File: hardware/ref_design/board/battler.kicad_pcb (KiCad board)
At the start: 4 copper layers, 70.4 x 151.2 mm, 123 parts, among them J1 TYPE-C-31-M-12, J2 S2B-PH-SM4-TB, J3 QD3525, J4 SPEAKER, J5 SWD, J6 UART, Q1 2N7002, SW1 P1 UP, SW10 P2 DOWN, SW11 P2 LEFT, SW12 P2 RIGHT, SW13 P2 A, SW14 P2 B, SW15 P2 X, SW16 P2 Y, SW17 PWR, SW18 BOOTSEL, SW19 RESET, SW2 P1 DOWN, SW3 P1 LEFT, SW4 P1 RIGHT, SW5 P1 A, SW6 P1 B, SW7 P1 X, SW8 P1 Y, SW9 P2 UP, U1 USBLC6-2SC6, U2 BQ24074RGTR, U3 TPS63001DRCR, U4 RP2350B, U5 W25Q128JVPIQ, U6 AP3156FVG-7, U7 MAX98357AETE+T, X1 12MHz

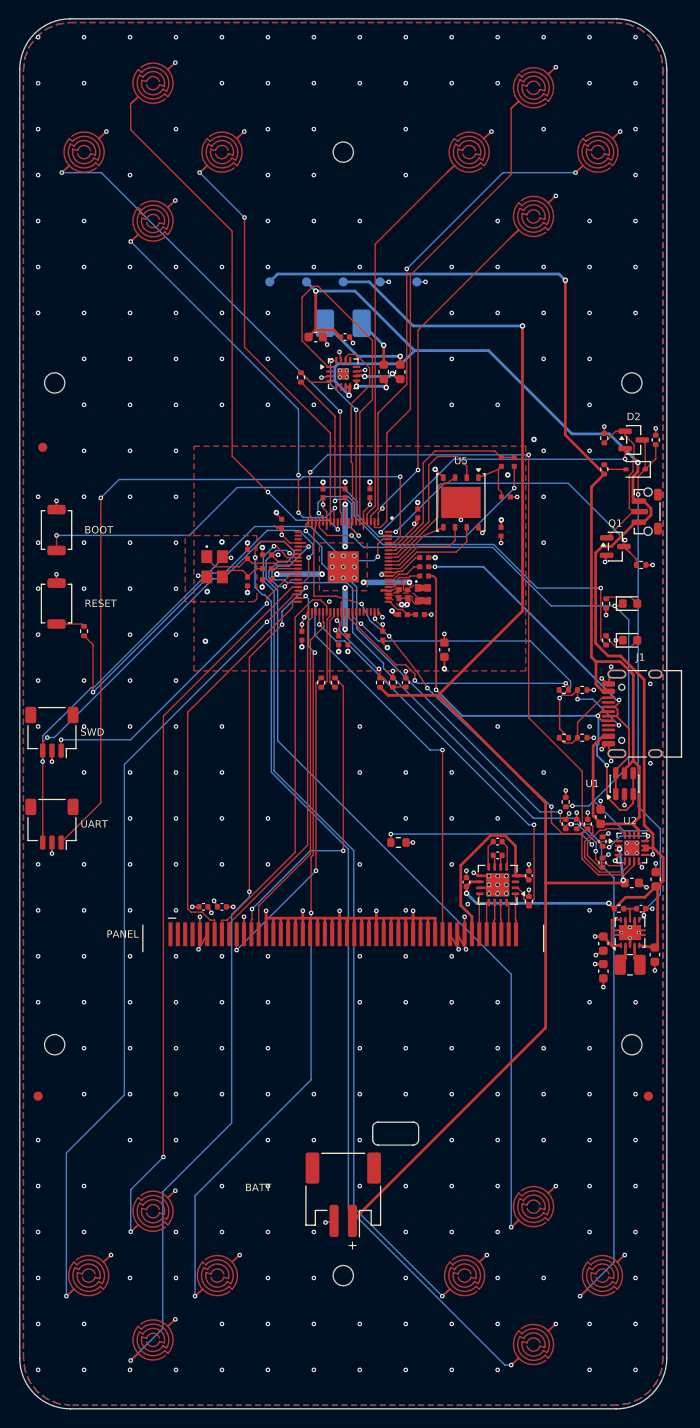
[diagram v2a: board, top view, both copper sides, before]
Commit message: 2-layer fork: board, case and docs for the approved cost changes
Board on two layers with every hole >= 0.3 mm (JLC's standard; smaller holes
cost about $40 an order), routed DRC-clean: 0 errors, 0 unconnected, 0 parity.
The RP2354B core is Raspberry Pi's 2-layer layout; its 3V3 pour sits inside
the chip's pads, fenced from the router, and every 3V3 pin stubs into it. GND
is poured on both layers and left out of Freerouting's job; 3V3 is routed.
USB series resistors are 22 ohm 0402 in Raspberry Pi's spots (a 27 ohm 0603
doesn't fit); UART1 on GPIO20/21 and seat 1's right on GPIO23 escape the
crystal's corner. route.py --finish closes what a full run leaves open.

Case 15 mm thick for the 503450 cell; the lid snaps on six hooks, six pins
locate the board; no lens, light pipes or power cap. Fit check: 90 parts, no
collisions. BOM split into factory (about $15.10 a unit) and self-assembled
(about $14-18); assembly, bring-up, pin map and design review updated.

Co-Authored-By: Claude Opus 5.5 <noreply@anthropic.com>
Claude-Session: https://claude.ai/code/session_01KGgEu3CbFtCsvHRQgAFiCN
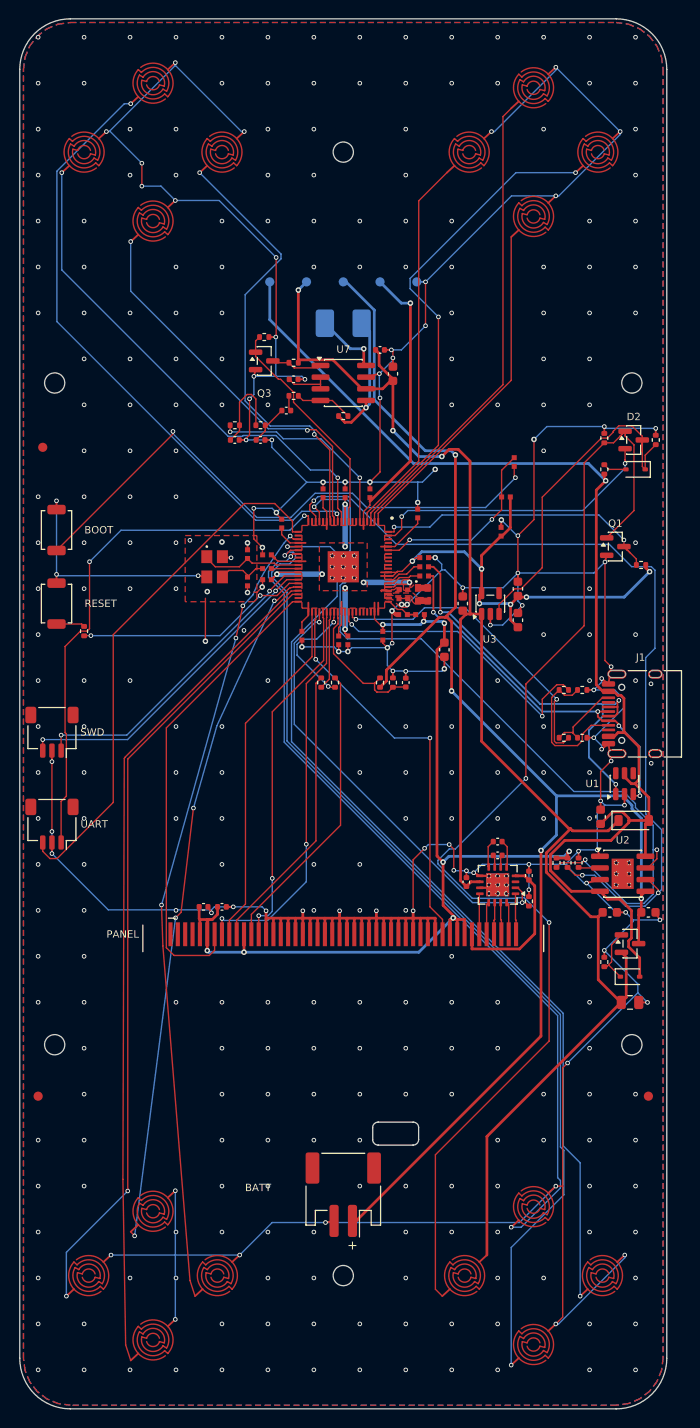
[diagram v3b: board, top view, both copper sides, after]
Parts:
- removed C4: 100n, Capacitor_SMD:C_0402_1005Metric
- removed D1: amber, LED_SMD:LED_0603_1608Metric
- removed D4: red, LED_SMD:LED_0603_1608Metric
- removed FB1, FB2: 120R@100MHz, Inductor_SMD:L_0603_1608Metric
- removed L1: 2.2u, Inductor_SMD:L_1008_2520Metric
- removed R11, R27: 1k, Resistor_SMD:R_0402_1005Metric
- removed R12: 100, Resistor_SMD:R_0402_1005Metric
- removed R24: 0, battler:R_0402_1005Metric_RPi
- removed R7, R8: 100k, Resistor_SMD:R_0402_1005Metric
- removed RT1: 10k B3380, Resistor_SMD:R_0603_1608Metric
- removed SW17: PWR, battler:SW_Alps_SKRTLAE010_Pullback
- removed U5: W25Q128JVPIQ, Package_SON:WSON-8-1EP_6x5mm_P1.27mm_EP3.4x4.3mm
- added C37: 10n, Capacitor_SMD:C_0402_1005Metric, F.Cu at (88.2, 70.2)
- added C38: 10n, Capacitor_SMD:C_0402_1005Metric, F.Cu at (91.0, 70.2)
- added C39: 220n, Capacitor_SMD:C_0402_1005Metric, F.Cu at (93.8, 67.0)
- added C40: 1u, Capacitor_SMD:C_0402_1005Metric, F.Cu at (94.6, 63.6)
- added C9: 22u, Capacitor_SMD:C_0805_2012Metric, F.Cu at (131.2, 131.4)
- added D5: B5819W, Diode_SMD:D_SOD-123, F.Cu at (131.6, 111.6)
- added D6: BAT54WS, Diode_SMD:D_SOD-323, F.Cu at (131.2, 128.6)
- added Q2: AO3401A, Package_TO_SOT_SMD:SOT-23, F.Cu at (131.2, 125.0)
- added Q3: 2N7002, Package_TO_SOT_SMD:SOT-23, F.Cu at (91.4, 61.6)
- added R33: 1k, Resistor_SMD:R_0402_1005Metric, F.Cu at (91.0, 68.6)
- added R34: 20k, Resistor_SMD:R_0402_1005Metric, F.Cu at (94.6, 65.4)
- added R35: 20k, Resistor_SMD:R_0402_1005Metric, F.Cu at (100.0, 67.6)
- added R36: 100k, Resistor_SMD:R_0402_1005Metric, F.Cu at (94.6, 61.8)
- added R37: 100k, Resistor_SMD:R_0402_1005Metric, F.Cu at (91.4, 59.0)
- C3: value 4.7u -> 10u
- R21, R22: value 27 -> 22
- R32: value 47k -> 1k
- R5: value 1.2k -> 2.4k
- R6: value 1.2k -> 10k
- SW8: value P1 Y -> P1 Y / PWR
- U1: value USBLC6-2SC6 -> SRV05-4
- U2: value BQ24074RGTR -> TP4056-42-ESOP8; footprint Package_DFN_QFN:VQFN-16-1EP_3x3mm_P0.5mm_EP1.6x1.6mm_ThermalVias -> battler:SOIC-8-1EP_3.9x4.9mm_P1.27mm_EP2.41x3.3mm_ThermalVias_0.3mm
- U3: value TPS63001DRCR -> ME6211C33M5G; footprint Package_SON:Texas_DRC0010J_ThermalVias -> Package_TO_SOT_SMD:SOT-23-5
- U4: value RP2350B -> RP2354B
- U7: value MAX98357AETE+T -> FM8002A; footprint Package_DFN_QFN:TQFN-16-1EP_3x3mm_P0.5mm_EP1.23x1.23mm_ThermalVias -> Package_SO:SOIC-8_3.9x4.9mm_P1.27mm
- moved C5 43.5 mm to (113.0, 88.0), turned to 90 degrees
- moved C6 39.7 mm to (119.0, 86.4), turned to 90 degrees
- moved C7 39.3 mm to (119.0, 89.8), turned to 90 degrees
- moved U3 38.9 mm to (116.0, 88.0)
- moved R6 10.8 mm to (128.4, 127.0)
- moved C34 9.30 mm to (105.4, 63.0), turned to 90 degrees
- moved R32 8.88 mm to (88.2, 68.6), turned to 0 degrees
- moved R10 6.68 mm to (123.2, 116.2)
- moved C2 6.16 mm to (129.0, 121.6), turned to 0 degrees
- moved R9 4.74 mm to (124.4, 116.2)
- moved C35 4.05 mm to (104.0, 60.4)
- moved C3 3.67 mm to (133.2, 121.6)
- moved R5 3.47 mm to (125.6, 116.2)
- moved U2 2.97 mm to (130.4, 117.4)
- moved U7 1.00 mm to (100.0, 64.0)
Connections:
- D2 pad 1: /Power/PWR_BTN_RAW -> PWR_BTN_RAW
- Q1 pad 1: /Power/PWR_BTN_RAW -> PWR_BTN_RAW
- R13 pad 1: /Power/PWR_BTN_RAW -> PWR_BTN_RAW
- R23 pad 2: /MCU/FLASH_SS -> QSPI_SS
- R32 pad 1: AMP_SD -> AUDIO_PWM
- R32 pad 2: /Audio/AMP_SD_MODE -> /Audio/AUDIO_F1
- R5 pad 1: /USB_Charger/ILIM -> /USB_Charger/CHG_PROG
- R6 pad 1: /USB_Charger/ISET -> /USB_Charger/LS_GATE
- R9 pad 1: VIN_GOOD_N -> CHG_DONE_N
- SW8 pad 1: P1_Y -> PWR_BTN_RAW
- SW8 pad 2: GND -> VSYS
- U1 pad 4: USB_DM -> (no net)
- U1 pad 6: USB_DP -> (no net)
- U2 pad 1: /USB_Charger/TS -> GND
- U2 pad 2: VBAT -> /USB_Charger/CHG_PROG
- U2 pad 3: VBAT -> GND
- U2 pad 4: GND -> VBUS
- U2 pad 5: CHG_EN2 -> VBAT
- U2 pad 6: CHG_EN1 -> CHG_DONE_N
- U2 pad 7: VIN_GOOD_N -> CHG_STAT_N
- U2 pad 8: GND -> VBUS
- U2 pad 9: CHG_STAT_N -> GND
- U3 pad 1: +3V3 -> VSYS
- U3 pad 2: /Power/BB_L2 -> GND
- U3 pad 3: GND -> /Power/PWR_EN
- U3 pad 4: /Power/BB_L1 -> (no net)
- U3 pad 5: VSYS -> +3V3
- U4 pad 16: STATUS_LED -> (no net)
- U4 pad 18: VIN_GOOD_N -> CHG_DONE_N
- U4 pad 19: CHG_EN1 -> (no net)
- U4 pad 20: CHG_EN2 -> UART_TX
- U4 pad 21: (no net) -> UART_RX
- U4 pad 23: (no net) -> P1_RIGHT
- U4 pad 28: P1_Y -> (no net)
- U4 pad 39: P1_RIGHT -> (no net)
- U4 pad 6: I2S_DIN -> AUDIO_PWM
- U4 pad 7: I2S_BCLK -> (no net)
- U4 pad 70: /MCU/QSPI_SD3 -> (no net)
- U4 pad 71: /MCU/QSPI_SCLK -> (no net)
- U4 pad 72: /MCU/QSPI_SD0 -> (no net)
- U4 pad 73: /MCU/QSPI_SD2 -> (no net)
- U4 pad 74: /MCU/QSPI_SD1 -> (no net)
- U4 pad 77: UART_TX -> (no net)
- U4 pad 78: UART_RX -> (no net)
- U4 pad 8: I2S_LRCLK -> (no net)
- U4 pad 9: AMP_SD -> AMP_EN
- U7 pad 1: I2S_DIN -> /Audio/AMP_SHDN
- U7 pad 2: (no net) -> /Audio/AMP_BYP
- U7 pad 3: GND -> /Audio/AMP_BYP
- U7 pad 4: /Audio/AMP_SD_MODE -> /Audio/AMP_INN
- U7 pad 5: (no net) -> /Audio/SPK_P
- U7 pad 6: (no net) -> VSYS
- U7 pad 7: VSYS -> GND
- U7 pad 8: VSYS -> /Audio/SPK_N
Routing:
- net GND: track 153.9 -> 692.9 mm, vias 355 -> 361
- net +3V3: track 75.6 -> 218.9 mm, vias 35 -> 15
- net PWR_BTN_RAW: track 0.00 -> 133.7 mm, vias 0 -> 2
- net P1_Y: track 94.5 -> 0.00 mm, vias 2 -> 0
- net CHG_DONE_N: track 0.00 -> 94.2 mm, vias 0 -> 3
- net CHG_EN1: track 86.1 -> 0.00 mm, vias 2 -> 0
- net VIN_GOOD_N: track 61.0 -> 0.00 mm, vias 4 -> 0
- net CHG_EN2: track 57.3 -> 0.00 mm, vias 4 -> 0
- net STATUS_LED: track 44.8 -> 0.00 mm, vias 2 -> 0
- net I2S_DIN: track 39.9 -> 0.00 mm
- net VSYS: track 157.3 -> 190.0 mm, vias 5 -> 3
- net /USB_Charger/TS: track 26.3 -> 0.00 mm, vias 2 -> 0
- net AMP_EN: track 0.00 -> 24.7 mm
- net AMP_SD: track 22.4 -> 0.00 mm, vias 2 -> 0
- net UART_TX: track 80.9 -> 58.9 mm
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- removed copper zone on In2.Cu, net +3V3
- removed copper zone on In1.Cu, net GND
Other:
- copper layers 4 -> 2
- board text added: "2 LAYERS 1.6 MM ENIG"
- board text removed: "4 LAYERS 1.6 MM ENIG"

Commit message: Reference design: plug-in ER-TFT035IPS-6 panel, pins and pin escapes for 2 layers
- Panel: EastRising ER-TFT035IPS-6 (ILI9488, 320x480 IPS) on a Hirose FH12-50S
  ZIF connector (J3) that JLC places, instead of the QD3525's hand-soldered tail.
  Case panel/FPC geometry, fit check (FPC zones), backlight sinks paired onto
  its two cathode pins, docs and BOM updated. Prices from both shops' carts:
  about $14.20 a unit at 10 with shipping.
- Pins reassigned for two layers: each faces where its net goes, in fan-out
  order (seat 1's face buttons, panel reset, backlight and ADC inputs on
  GPIO40-47; seat 1's cross and the panel's TE on GPIO28-32).
- build_pcb.copy_escapes: Raspberry Pi's own routing out of the RP2354B's pins,
  copied with the core and locked, so no pin gets boxed in by its neighbours.
  The board now routes completely in about 10 minutes.
- route.py: loose tracks are trimmed back to their last real join instead of
  deleted (Freerouting meets stubs part-way along), T-joins are split and
  duplicate tracks dropped; Freerouting routes to +5 um clearance and a 0.12 mm
  inset outline (it rounded under 0.15 mm and hugged the board edge).
- MCU sheet region widened for the longer labels; datasheet list updated for
  the 2-layer parts; old panel landing footprint/tool and the unused side
  switch footprint removed.

Checks: netlist PASS (122 parts, 115 nets), ERC 0, DRC 0 errors / 0
unconnected / 0 parity (2 cosmetic silk warnings), holes 0.3/0.6/0.65/2.2 mm,
fit PASS on 91 parts.

Co-Authored-By: Claude Opus 5.5 <noreply@anthropic.com>
Claude-Session: https://claude.ai/code/session_01KGgEu3CbFtCsvHRQgAFiCN
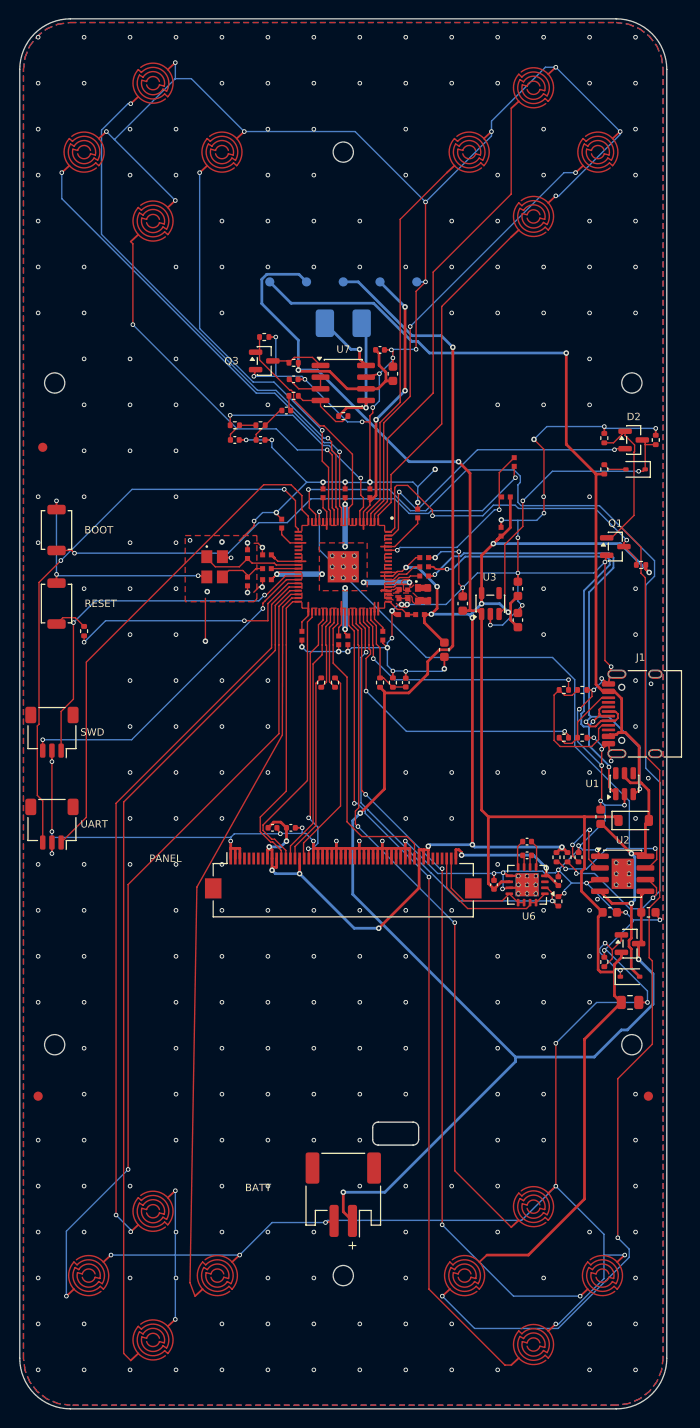
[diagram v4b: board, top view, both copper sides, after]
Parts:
- J3: value QD3525 -> FH12-50S-0.5SH(55); footprint battler:QD3525_FPC_1x48_P0.80mm_Solder -> Connector_FFC-FPC:Hirose_FH12-50S-0.5SH_1x50-1MP_P0.50mm_Horizontal
- moved C29 11.4 mm to (92.3, 112.4)
- moved C30 11.4 mm to (94.3, 112.4)
- moved J3 6.39 mm to (100.0, 117.6)
- moved C32 3.26 mm to (123.4, 118.2)
- moved C33 3.20 mm to (120.0, 115.4)
- moved C36 3.20 mm to (120.0, 113.9)
- moved R31 3.20 mm to (123.4, 120.4)
- moved U6 3.20 mm to (120.0, 118.6)
- moved C31 3.01 mm to (116.4, 118.6)
- moved R10 0.60 mm to (123.2, 115.6)
- moved R5 0.60 mm to (125.6, 115.6)
- moved R9 0.60 mm to (124.4, 115.6)
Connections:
- J3 pad 1: (no net) -> GND
- J3 pad 10: /Display/LCD_SCK -> +3V3
- J3 pad 12: /Display/LCD_MOSI -> LCD_TE
- J3 pad 13: LCD_MISO -> LCD_CS
- J3 pad 14: GND -> LCD_DC
- J3 pad 15: GND -> /Display/LCD_SCK
- J3 pad 16: GND -> +3V3
- J3 pad 17: GND -> /Display/LCD_MOSI
- J3 pad 18: GND -> LCD_MISO
- J3 pad 2: (no net) -> GND
- J3 pad 3: (no net) -> GND
- J3 pad 38: LCD_RST -> GND
- J3 pad 39: +3V3 -> GND
- J3 pad 40: +3V3 -> GND
- J3 pad 41: +3V3 -> LCD_RST
- J3 pad 42: /Display/LED_A -> +3V3
- J3 pad 43: /Display/LED_K1 -> +3V3
- J3 pad 44: /Display/LED_K2 -> +3V3
- J3 pad 45: /Display/LED_K3 -> (no net)
- J3 pad 46: /Display/LED_K4 -> (no net)
- J3 pad 47: /Display/LED_K5 -> (no net)
- J3 pad 48: /Display/LED_K6 -> /Display/LED_K2
- J3 pad 5: +3V3 -> (no net)
- J3 pad 6: +3V3 -> (no net)
- J3 pad 7: LCD_TE -> (no net)
- J3 pad 8: LCD_CS -> GND
- J3 pad 9: LCD_DC -> +3V3
- U4 pad 23: P1_RIGHT -> (no net)
- U4 pad 25: P1_A -> (no net)
- U4 pad 26: P1_B -> (no net)
- U4 pad 27: P1_X -> (no net)
- U4 pad 39: (no net) -> P1_RIGHT
- U4 pad 42: LCD_DC -> LCD_CS
- U4 pad 43: LCD_RST -> (no net)
- U4 pad 44: BL_SDI -> (no net)
- U4 pad 46: LCD_CS -> LCD_DC
- U4 pad 49: VBAT_SENSE -> LCD_RST
- U4 pad 52: CC1_SENSE -> P1_B
- U4 pad 53: CC2_SENSE -> P1_X
- U4 pad 54: (no net) -> P1_A
- U4 pad 55: (no net) -> BL_SDI
- U4 pad 56: (no net) -> CC2_SENSE
- U4 pad 57: (no net) -> CC1_SENSE
- U4 pad 58: (no net) -> VBAT_SENSE
- U6 pad 1: /Display/LED_K6 -> /Display/LED_K2
- U6 pad 13: /Display/LED_K2 -> /Display/LED_K1
- U6 pad 14: /Display/LED_K3 -> /Display/LED_K1
- U6 pad 15: /Display/LED_K4 -> /Display/LED_K2
- U6 pad 16: /Display/LED_K5 -> /Display/LED_K2
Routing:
- net LCD_TE: track 51.5 -> 31.1 mm
- net P1_B: track 109.7 -> 91.0 mm
- net USB_DM: track 40.8 -> 58.4 mm, vias 4 -> 3
- net P1_X: track 92.6 -> 75.6 mm
- net P1_A: track 103.9 -> 90.1 mm, vias 2 -> 4
- net GND: track 692.9 -> 679.8 mm, vias 361 -> 357
- net LCD_CS: track 43.0 -> 30.3 mm, vias 2 -> 0
- net CHG_STAT_N: track 87.9 -> 75.6 mm
- net /Display/LED_K2: track 3.62 -> 15.6 mm
- net /Display/LCD_SCK: track 31.7 -> 20.8 mm
- net /Display/LCD_MOSI: track 32.2 -> 21.6 mm
- net LCD_DC: track 38.8 -> 28.5 mm
- net LCD_MISO: track 38.6 -> 28.6 mm
- net VBUS: track 134.2 -> 124.6 mm, vias 1 -> 3
- net LCD_RST: track 43.1 -> 33.6 mm, vias 2 -> 0
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
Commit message: Reference design: audit round 1 fixes (USB ESD reference, PWR_EN pull-down)
From an independent audit of the 2-layer board:
- SRV05-4 REF (U1 pin 5) moves from VBUS to 3V3. On VBUS, with no cable in,
  the MCU's D+ pull-up (always on in BOOTSEL mode) fed VBUS through the D+
  steering diode to about 2.7 V: PWR_EN stayed up, so the device could not
  turn off, and the load-sharing FET was left half on.
- R15 (PWR_EN pull-down) 100k -> 10k, so D5's reverse leakage into the VBUS
  node can't lift the ME6211's CE to 1.0 V when warm.
- J6 (UART) turned 180 degrees: its mouth faced J5's back 5 mm away.
- Lid: the panel's locating frame gets 0.8 mm clearance (panel_fit), not 0.4.
- Docs: ILI9488 reads at 5 MHz or less, TP4056 current 460-500 mA and its
  145 C thermal limit, how 3V3 reaches the core pour, FPC insertion depth and
  expected slack, JLC's 374 solder joints, board size as quoted.

Checks: netlist PASS, ERC 0, DRC 0 errors / 0 unconnected / 0 parity
(2 cosmetic silk warnings), fit PASS on 91 parts.

Co-Authored-By: Claude Opus 5.5 <noreply@anthropic.com>
Claude-Session: https://claude.ai/code/session_01KGgEu3CbFtCsvHRQgAFiCN
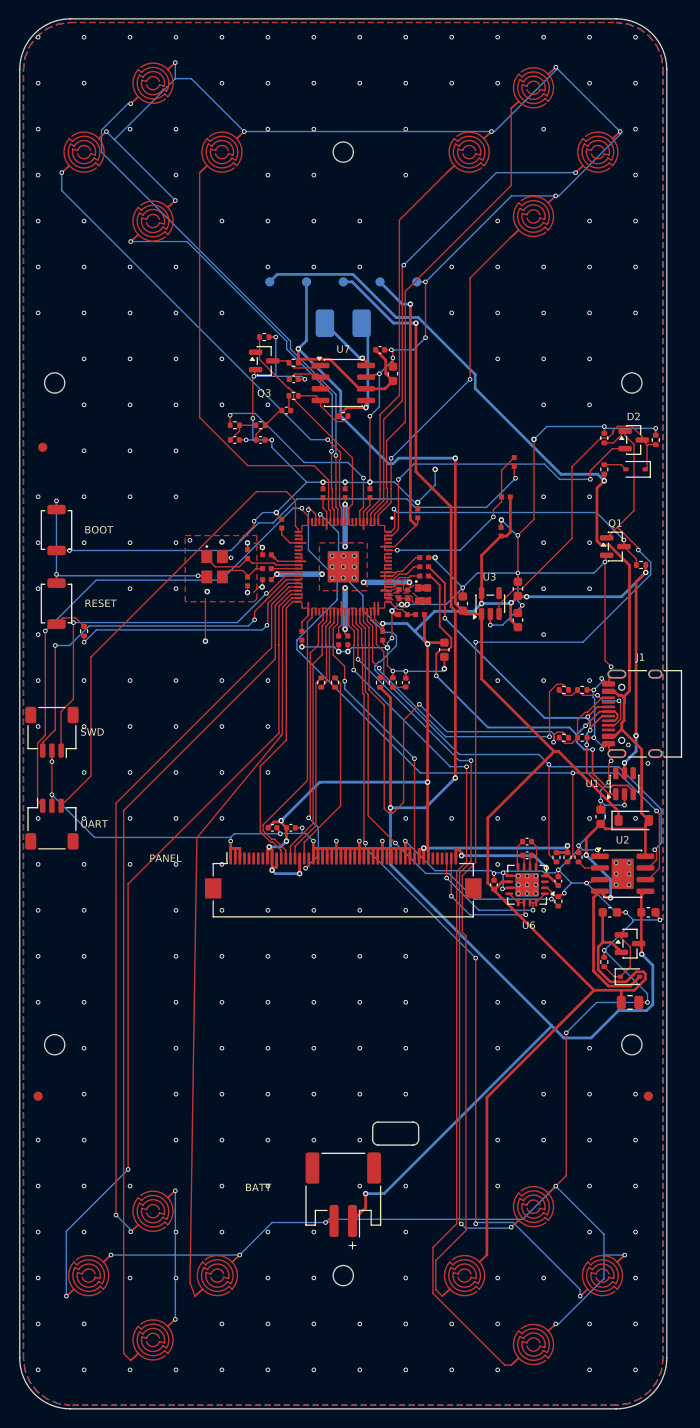
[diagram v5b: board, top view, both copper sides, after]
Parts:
- R15: value 100k -> 10k
- turned J6 to 0 degrees
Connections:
- U1 pad 5: VBUS -> +3V3
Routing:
- net CC2_SENSE: track 33.4 -> 56.1 mm
- net +3V3: track 209.6 -> 227.8 mm, vias 19 -> 17
- net CHG_DONE_N: track 103.5 -> 85.5 mm
- net UART_RX: track 64.9 -> 51.2 mm, vias 2 -> 0
- net GND: track 679.8 -> 666.4 mm
- net USB_DP: track 54.0 -> 42.3 mm, vias 3 -> 4
- net USB_DM: track 58.4 -> 49.4 mm
- net VSYS: track 183.7 -> 191.4 mm
- net CC1_SENSE: track 28.7 -> 36.0 mm
- net /USB_Charger/CHG_PROG: track 9.51 -> 2.60 mm, vias 2 -> 0
- net PWR_BTN_RAW: track 126.7 -> 120.2 mm
- net SWDIO: track 36.5 -> 41.9 mm
- net VBAT: track 166.6 -> 171.8 mm, vias 4 -> 5
- net PWR_BTN_N: track 37.9 -> 33.0 mm
- net /USB_Charger/CC1: track 16.0 -> 11.2 mm, vias 0 -> 2
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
